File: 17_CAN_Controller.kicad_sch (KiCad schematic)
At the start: 15 parts

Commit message: maj réduction de taille
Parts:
- removed ? (x8): Conn_01x01, Chimere_mods:Castellated_conn, symbol Connector_Generic:Conn_01x01
- added J1: Conn_01x08, Connector_PinHeader_2.54mm:PinHeader_1x08_P2.54mm_Vertical, symbol Connector_Generic:Conn_01x08
- added J2: Conn_01x01, Connector_PinHeader_2.54mm:PinHeader_1x01_P2.54mm_Vertical, symbol Connector_Generic:Conn_01x01
- gave numbers to parts that had none: 7
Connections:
- net 5V: now also J1.1 (Pin_1)
- net CAN_RX: now also J1.3 (Pin_3)
- net CAN_TX: now also J1.2 (Pin_2)
- net CS: now also J1.5 (Pin_5)
- net GND: now also J1.4 (Pin_4), J2.1 (Pin_1)
- net MISO: now also J1.7 (Pin_7)
- net MOSI: now also J1.6 (Pin_6)
- net SCK: now also J1.8 (Pin_8)

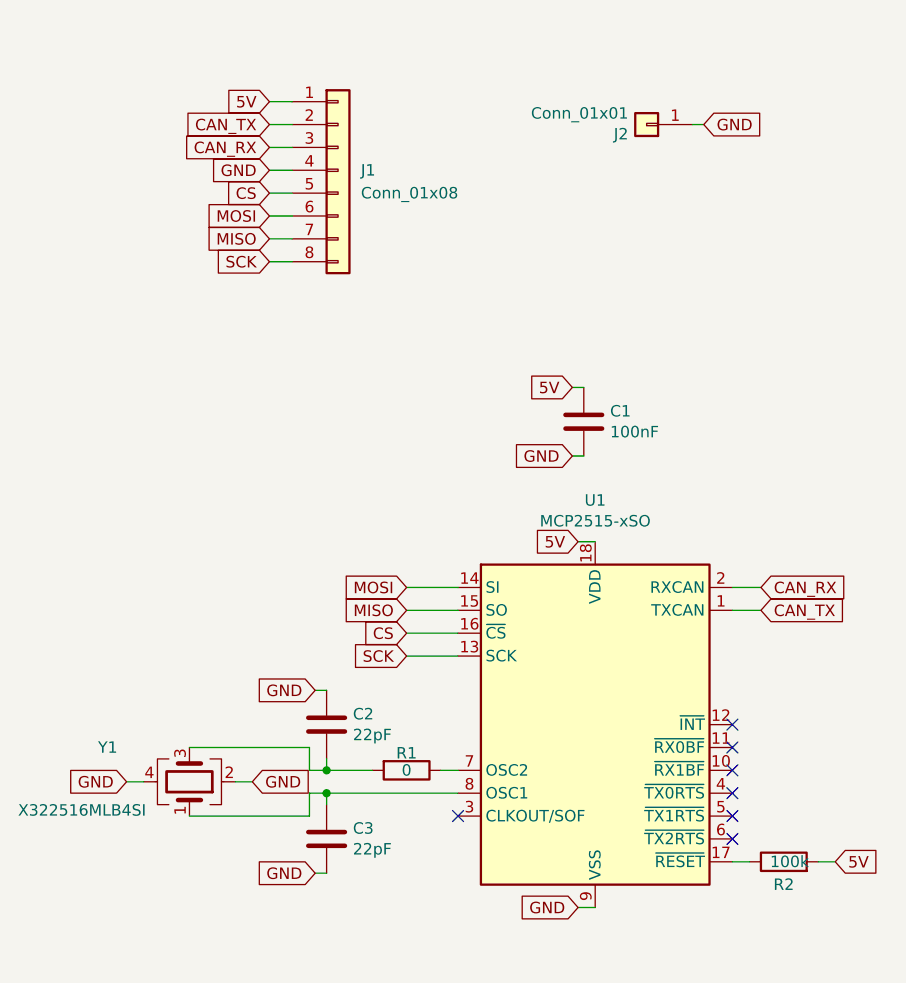
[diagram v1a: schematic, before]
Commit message: maj kicad 6 jlcpcb
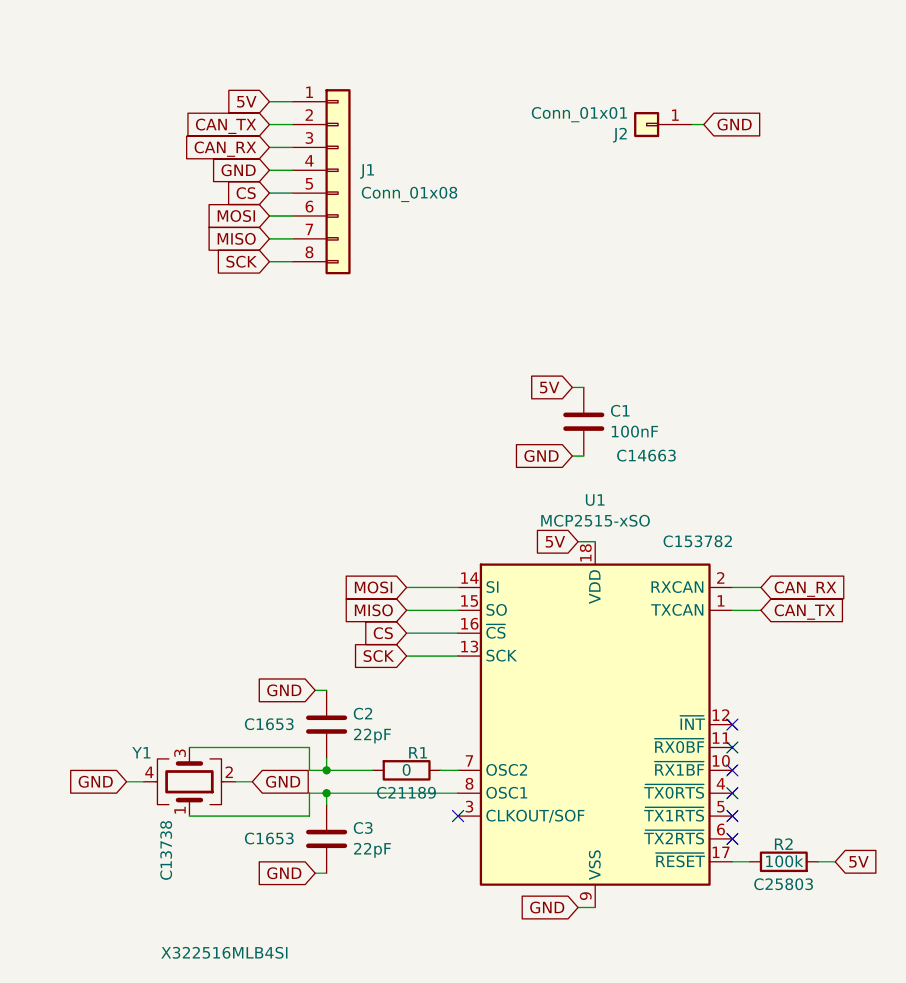
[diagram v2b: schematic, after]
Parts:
- C1: LCSC (none) -> C14663
- C2, C3: LCSC (none) -> C1653
- R1: LCSC (none) -> C21189
- R2: LCSC (none) -> C25803
- U1: LCSC (none) -> C153782
- Y1: LCSC (none) -> C13738
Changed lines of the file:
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@@
     )
   )
-  (symbol (lib_id "Device:R") (at 152.4 114.935 90) (unit 1)
+  (symbol (lib_name "R_1") (lib_id "Device:R") (at 152.4 114.935 90) (unit 1)
     (in_bom yes) (on_board yes)
-    (property "Reference" "R2" (id 0) (at 152.4 117.475 90))
-    (property "Value" "100k" (id 1) (at 153.035 114.935 90))
-    (property "Footprint" "Resistor_SMD:R_0603_1608Metric_Pad1.05x0.95mm_HandSolder" (id 2) (at 152.4 116.713 90)
+    (property "Reference" "R2" (id 0) (at 152.4 113.03 90))
+    (property "Value" "100k" (id 1) (at 152.4 114.935 90))
+    (property "Footprint" "Resistor_SMD:R_0603_1608Metric_Pad1.05x0.95mm_HandSolder" (id 2) (at 153.67 112.395 90)
       (effects (font (size 1.27 1.27)) hide)
     )
-    (property "Datasheet" "C25803" (id 3) (at 152.4 114.935 0)
+    (property "Datasheet" "-" (id 3) (at 152.4 114.935 0)
       (effects (font (size 1.27 1.27)) hide)
     )
+    (property "LCSC" "C25803" (id 4) (at 152.4 117.475 90))
     (pin "1")
     (pin "2")
   )
-  (symbol (lib_id "Device:C") (at 130.175 66.04 0) (unit 1)
+  (symbol (lib_name "C_1") (lib_id "Device:C") (at 130.175 66.04 0) (unit 1)
     (in_bom yes) (on_board yes)
     (property "Reference" "C1" (id 0) (at 133.096 64.8716 0)
@@
       (effects (font (size 1.27 1.27)) hide)
     )
-    (property "Datasheet" "C14663" (id 3) (at 130.175 66.04 0)
+    (property "Datasheet" "~" (id 3) (at 130.175 66.04 0)
       (effects (font (size 1.27 1.27)) hide)
     )
+    (property "LCSC" "C14663" (id 4) (at 137.16 69.85 0))
     (pin "1")
     (pin "2")
@@
       (effects (font (size 1.27 1.27) italic) hide)
     )
-    (property "Datasheet" "C153782" (id 3) (at 133.985 120.015 0)
+    (property "Datasheet" "-" (id 3) (at 133.985 120.015 0)
       (effects (font (size 1.27 1.27)) hide)
     )
+    (property "LCSC" "C153782" (id 4) (at 142.875 79.375 0))
     (pin "1")
     (pin "10")
@@
   (symbol (lib_id "Device:R") (at 110.49 104.775 270) (unit 1)
     (in_bom yes) (on_board yes)
-    (property "Reference" "R1" (id 0) (at 110.49 102.87 90))
+    (property "Reference" "R1" (id 0) (at 111.76 102.87 90))
     (property "Value" "0" (id 1) (at 110.49 104.775 90))
-    (property "Footprint" "Resistor_SMD:R_0603_1608Metric" (id 2) (at 110.49 102.997 90)
+    (property "Footprint" "Resistor_SMD:R_0603_1608Metric" (id 2) (at 111.76 102.235 90)
       (effects (font (size 1.27 1.27)) hide)
     )
-    (property "Datasheet" "C21189" (id 3) (at 110.49 104.775 0)
+    (property "Datasheet" "-" (id 3) (at 110.49 104.775 0)
       (effects (font (size 1.27 1.27)) hide)
     )
+    (property "LCSC" "C21189" (id 4) (at 110.49 107.315 90))
     (pin "1")
     (pin "2")
   )
-  (symbol (lib_id "Device:C") (at 101.6 99.695 0) (unit 1)
+  (symbol (lib_name "C_2") (lib_id "Device:C") (at 101.6 99.695 0) (unit 1)
     (in_bom yes) (on_board yes)
     (property "Reference" "C2" (id 0) (at 104.521 98.5266 0)
@@
       (effects (font (size 1.27 1.27)) hide)
     )
-    (property "Datasheet" "C1653" (id 3) (at 101.6 99.695 0)
+    (property "Datasheet" "-" (id 3) (at 101.6 99.695 0)
       (effects (font (size 1.27 1.27)) hide)
     )
+    (property "LCSC" "C1653" (id 4) (at 95.25 99.695 0))
     (pin "1")
     (pin "2")
@@
       (effects (font (size 1.27 1.27)) hide)
     )
-    (property "Datasheet" "C1653" (id 3) (at 101.6 112.395 0)
+    (property "Datasheet" "" (id 3) (at 101.6 112.395 0)
       (effects (font (size 1.27 1.27)) hide)
     )
+    (property "LCSC" "C1653" (id 4) (at 95.25 112.395 0))
     (pin "1")
     (pin "2")
@@
   (symbol (lib_id "Device:Crystal_GND24") (at 86.36 106.045 270) (mirror x) (unit 1)
     (in_bom yes) (on_board yes)
-    (property "Reference" "Y1" (id 0) (at 76.2 102.235 90)
+    (property "Reference" "Y1" (id 0) (at 80.01 102.87 90)
       (effects (font (size 1.27 1.27)) (justify left))
     )
-    (property "Value" "X322516MLB4SI" (id 1) (at 67.31 109.22 90)
+    (property "Value" "X322516MLB4SI" (id 1) (at 83.185 125.095 90)
       (effects (font (size 1.27 1.27)) (justify left))
     )
-    (property "Footprint" "Crystal:Crystal_SMD_3225-4Pin_3.2x2.5mm" (id 2) (at 86.36 106.045 0)
+    (property "Footprint" "Crystal:Crystal_SMD_3225-4Pin_3.2x2.5mm" (id 2) (at 81.28 108.585 0)
       (effects (font (size 1.27 1.27)) hide)
     )
-    (property "Datasheet" "C13738" (id 3) (at 86.36 106.045 0)
+    (property "Datasheet" "-" (id 3) (at 86.36 106.045 0)
       (effects (font (size 1.27 1.27)) hide)
     )
+    (property "LCSC" "C13738" (id 4) (at 83.82 113.665 0))
     (pin "1")
     (pin "2")

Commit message: maj librairies et silk
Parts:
- R2: footprint Resistor_SMD:R_0603_1608Metric_Pad1.05x0.95mm_HandSolder -> Resistor_SMD:R_0603_1608Metric
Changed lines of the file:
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@@
     )
   )
-  (symbol (lib_name "R_1") (lib_id "Device:R") (at 152.4 114.935 90) (unit 1)
+  (symbol (lib_id "Device:R") (at 152.4 114.935 90) (unit 1)
     (in_bom yes) (on_board yes)
     (property "Reference" "R2" (id 0) (at 152.4 113.03 90))
     (property "Value" "100k" (id 1) (at 152.4 114.935 90))
-    (property "Footprint" "Resistor_SMD:R_0603_1608Metric_Pad1.05x0.95mm_HandSolder" (id 2) (at 153.67 112.395 90)
-      (effects (font (size 1.27 1.27)) hide)
-    )
-    (property "Datasheet" "-" (id 3) (at 152.4 114.935 0)
-      (effects (font (size 1.27 1.27)) hide)
-    )
-    (property "LCSC" "C25803" (id 4) (at 152.4 117.475 90))
+    (property "Footprint" "Resistor_SMD:R_0603_1608Metric" (id 2) (at 153.67 112.395 90)
+      (effects (font (size 1.27 1.27)) hide)
+    )
+    (property "Datasheet" "~" (id 3) (at 152.4 114.935 0)
+      (effects (font (size 1.27 1.27)) hide)
+    )
+    (property "LCSC" "C25803" (id 4) (at 152.4 117.475 90)
+      (effects (font (size 1.27 1.27)) hide)
+    )
     (pin "1")
     (pin "2")
@@
       (effects (font (size 1.27 1.27)) hide)
     )
-    (property "LCSC" "C14663" (id 4) (at 137.16 69.85 0))
+    (property "LCSC" "C14663" (id 4) (at 137.16 69.85 0)
+      (effects (font (size 1.27 1.27)) hide)
+    )
     (pin "1")
     (pin "2")
@@
       (effects (font (size 1.27 1.27) italic) hide)
     )
-    (property "Datasheet" "-" (id 3) (at 133.985 120.015 0)
+    (property "Datasheet" "http://ww1.microchip.com/downloads/en/DeviceDoc/21801e.pdf" (id 3) (at 133.985 120.015 0)
       (effects (font (size 1.27 1.27)) hide)
     )
@@
       (effects (font (size 1.27 1.27)) hide)
     )
-    (property "Datasheet" "-" (id 3) (at 110.49 104.775 0)
-      (effects (font (size 1.27 1.27)) hide)
-    )
-    (property "LCSC" "C21189" (id 4) (at 110.49 107.315 90))
+    (property "Datasheet" "~" (id 3) (at 110.49 104.775 0)
+      (effects (font (size 1.27 1.27)) hide)
+    )
+    (property "LCSC" "C21189" (id 4) (at 110.49 107.315 90)
+      (effects (font (size 1.27 1.27)) hide)
+    )
     (pin "1")
     (pin "2")
@@
       (effects (font (size 1.27 1.27)) hide)
     )
-    (property "Datasheet" "-" (id 3) (at 101.6 99.695 0)
-      (effects (font (size 1.27 1.27)) hide)
-    )
-    (property "LCSC" "C1653" (id 4) (at 95.25 99.695 0))
+    (property "Datasheet" "~" (id 3) (at 101.6 99.695 0)
+      (effects (font (size 1.27 1.27)) hide)
+    )
+    (property "LCSC" "C1653" (id 4) (at 95.25 99.695 0)
+      (effects (font (size 1.27 1.27)) hide)
+    )
     (pin "1")
     (pin "2")
@@
       (effects (font (size 1.27 1.27)) hide)
     )
-    (property "Datasheet" "" (id 3) (at 101.6 112.395 0)
-      (effects (font (size 1.27 1.27)) hide)
-    )
-    (property "LCSC" "C1653" (id 4) (at 95.25 112.395 0))
+    (property "Datasheet" "~" (id 3) (at 101.6 112.395 0)
+      (effects (font (size 1.27 1.27)) hide)
+    )
+    (property "LCSC" "C1653" (id 4) (at 95.25 112.395 0)
+      (effects (font (size 1.27 1.27)) hide)
+    )
     (pin "1")
     (pin "2")
@@
       (effects (font (size 1.27 1.27)) hide)
     )
-    (property "Datasheet" "-" (id 3) (at 86.36 106.045 0)
+    (property "Datasheet" "~" (id 3) (at 86.36 106.045 0)
       (effects (font (size 1.27 1.27)) hide)
     )
@@
     )
     (path "/00000000-0000-0000-0000-000060784930"
-      (reference "R2") (unit 1) (value "100k") (footprint "Resistor_SMD:R_0603_1608Metric_Pad1.05x0.95mm_HandSolder")
+      (reference "R2") (unit 1) (value "100k") (footprint "Resistor_SMD:R_0603_1608Metric")
     )
     (path "/00000000-0000-0000-0000-000060b60157"
